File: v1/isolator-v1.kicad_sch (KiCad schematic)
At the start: 42 parts, among them J1 HOST, J2 PORT, Q1 2N7002, T1 750313638, U1 ADuM4165, U2 USBLC6-2SC6, U3 USBLC6-2SC6, U4 SN6505BDBV, U5 TLV76750DGNR, U6 TPS2553DBV, Y1 24M 8pF

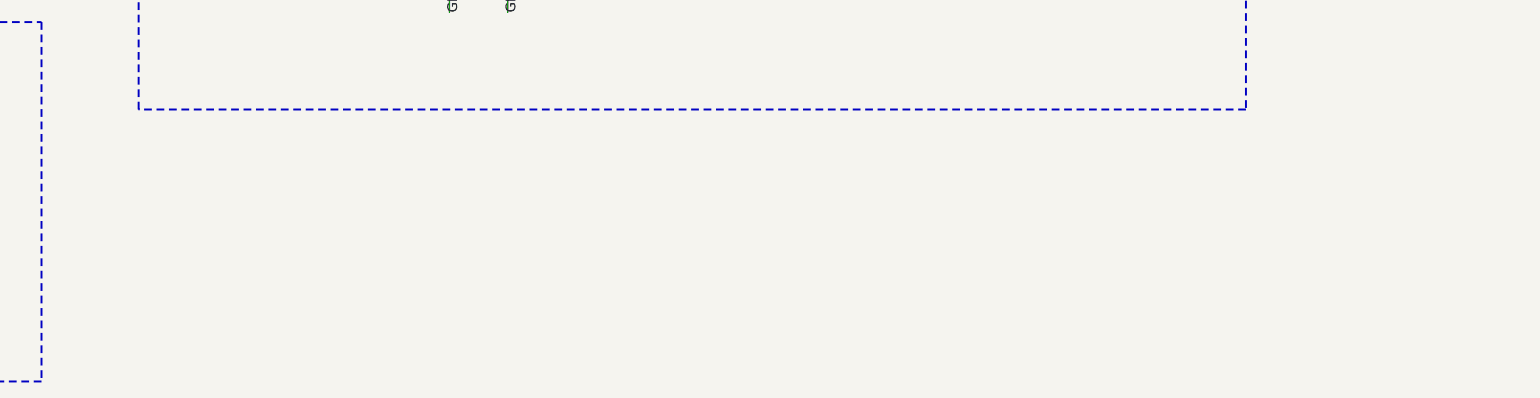
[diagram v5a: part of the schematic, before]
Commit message: feat(v1/sch): populated barrier stitching cap, PWR_FLAGs, ERC clean
- Place CY1 (Device:C, Songtian Q07F3Z102MA5B0S0N0, 1nF Y1 400VAC,
  isolator-lib:C_Disc_D7.0mm_W5.5mm_P14.00mm) bridging GND1/GND2 --
  populated, not DNP, per Task 2's part selection. Adds the Device:C
  lib_symbol (not previously embedded) and a dedicated section box with
  a note explaining the populated-vs-DNP rationale and warning against
  substituting v2's 2220 SMD part.
- Audit PWR_FLAGs: confirmed the existing four (GND1, GND2, VBUS_HOST,
  DCDC_RAW) are all required -- DCDC_RAW's flag was undocumented in the
  brief but is legitimate (D1/D2 rectifier pins are passive-typed, not
  a recognized ERC source), and VDD1 correctly has none (U1 pin 3 is
  power_out). No flags added or removed.
- Fix D3 Description: still said "PGOOD confirmed push-pull", now
  matches Task 5's "unspecified" reclassification.
- ERC: 0 errors, exit 0. One pre-existing warning carried forward
  (lib_symbol_mismatch on U4 SN6505BDBV, known library-version drift,
  same class already present in the v2 reference design) -- CY1
  introduces no new warnings.
- Isolation check: GND1/GND2 bridge only via U1, T1, CY1 (the
  now-expanded allow-list); CY1 confirmed present on both nets.
- Zero-overlap sweep: programmatic pairwise check over every label/text
  (lib_symbols cache excluded) plus full-sheet high-res render; no true
  overlaps (one heuristic false positive on a pre-existing, untouched
  label pair, visually confirmed clear).

Co-Authored-By: Claude Opus 5 <noreply@anthropic.com>
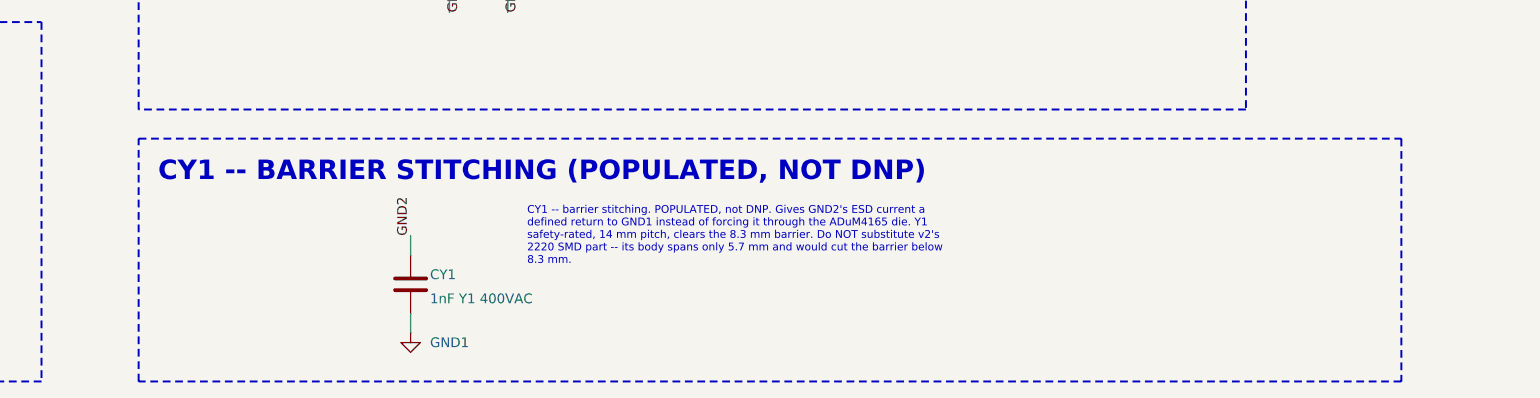
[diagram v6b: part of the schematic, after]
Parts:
- added CY1: 1nF Y1 400VAC, isolator-lib:C_Disc_D7.0mm_W5.5mm_P14.00mm, symbol Device:C
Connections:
- net GND1: now also CY1.2
- net GND2: now also CY1.1
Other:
- note added: "CY1 -- BARRIER STITCHING (POPULATED, NOT DNP)"
- note added: "CY1 -- barrier stitching. POPULATED, not DNP. Gives GND2's ESD current a defined return to GND1 instead of forcing it through the ADuM4165 die. Y1 safety-rated, 14 mm pitch, clears the 8.3 mm barrier. Do NOT substitute v2's 2220 SMD part -- its body spans only 5.7 mm and would cut the barrier below 8.3 mm."
